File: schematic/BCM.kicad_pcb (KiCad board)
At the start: 2 copper layers, 69 parts, among them P401 POWERCON, P402 KEYSWITCH, P403 CHARGESW, P601 BRUSA_CANCON, P602 A123_CANCON, P603 CON+, P604 CON-, P605 CONPRE, P606 UART, Q1 IRF7101PbF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

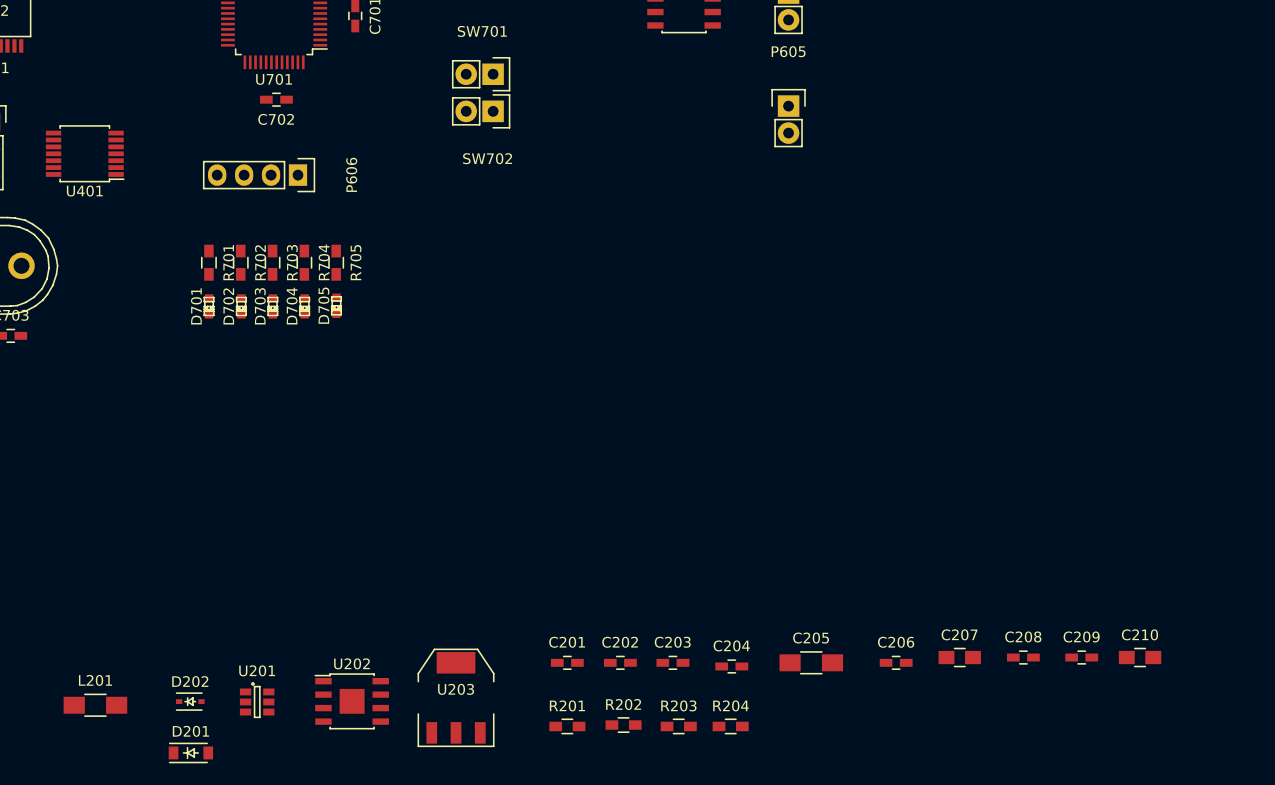
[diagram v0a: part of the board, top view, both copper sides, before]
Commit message: layout: most parts done, fill zones in progress
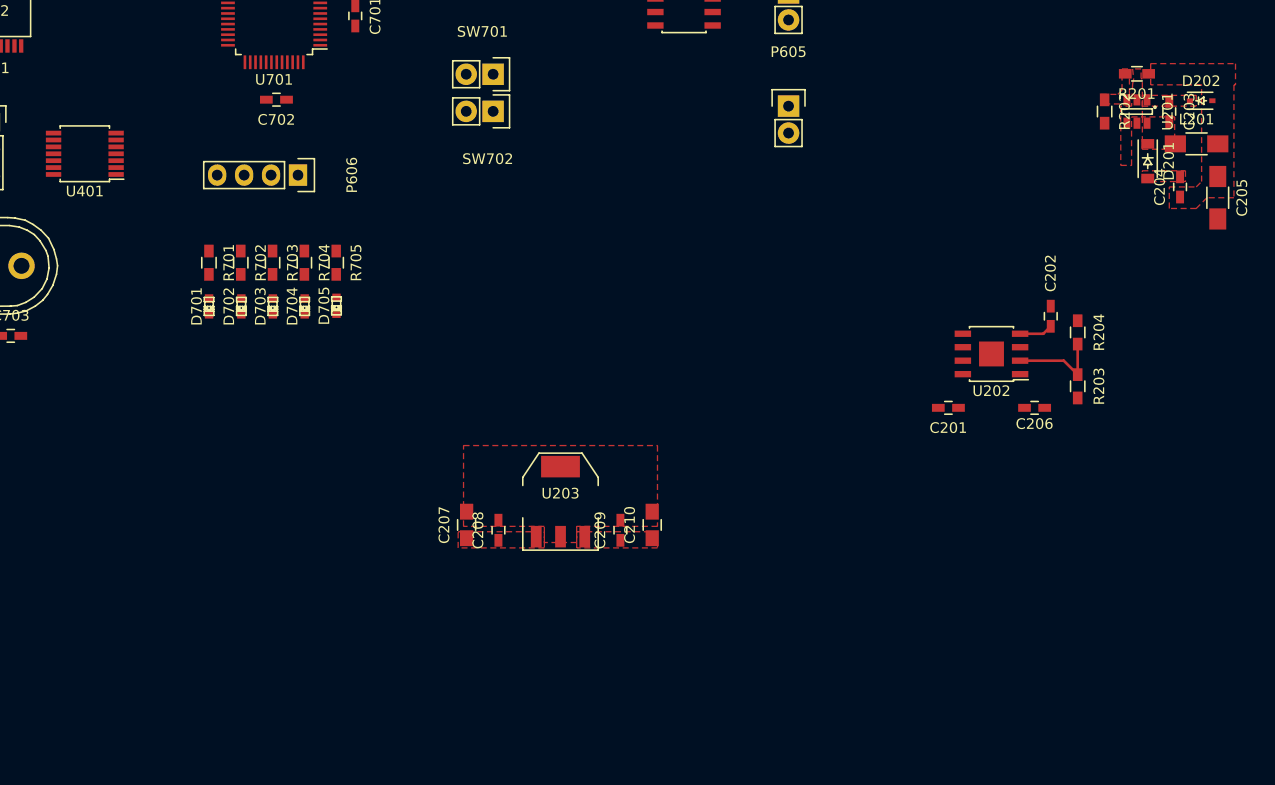
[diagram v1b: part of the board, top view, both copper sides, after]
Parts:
- moved L201 116.5 mm to (209.3, 131.1)
- moved D202 110.9 mm to (209.8, 127.0)
- moved D201 106.1 mm to (204.7, 132.7), turned to 270 degrees
- moved U201 99.9 mm to (203.7, 128.0), turned to 270 degrees
- moved R201 81.7 mm to (203.7, 124.5), turned to 180 degrees
- moved R202 73.5 mm to (200.7, 128.0), turned to 270 degrees
- moved C203 70.0 mm to (206.8, 128.0), turned to 270 degrees
- moved U202 68.6 mm to (190.0, 150.9), turned to 180 degrees
- moved C204 61.9 mm to (207.8, 135.1), turned to 90 degrees
- moved C205 58.2 mm to (211.3, 136.1), turned to 270 degrees
- moved C202 52.1 mm to (195.6, 147.3), turned to 90 degrees
- moved C208 50.9 mm to (143.5, 167.5), turned to 90 degrees
- moved R204 49.5 mm to (198.1, 148.8), turned to 90 degrees
- moved R203 49.4 mm to (198.1, 153.9), turned to 90 degrees
- moved C207 48.2 mm to (140.5, 167.0), turned to 90 degrees
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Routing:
- net /Power/12V0_FB: track 0.00 -> 8.85 mm
- net /Power/12V0_SS: track 0.00 -> 3.18 mm
- added copper zone on F.Cu, net +5V
- added copper zone on F.Cu, net /Power/5V0_BOOST
- added copper zone on F.Cu, net /Power/5V0_FB
- added copper zone on F.Cu, net /Power/5V0_L
- added copper zone on F.Cu, net GND
- added copper zone on F.Cu, net VCC

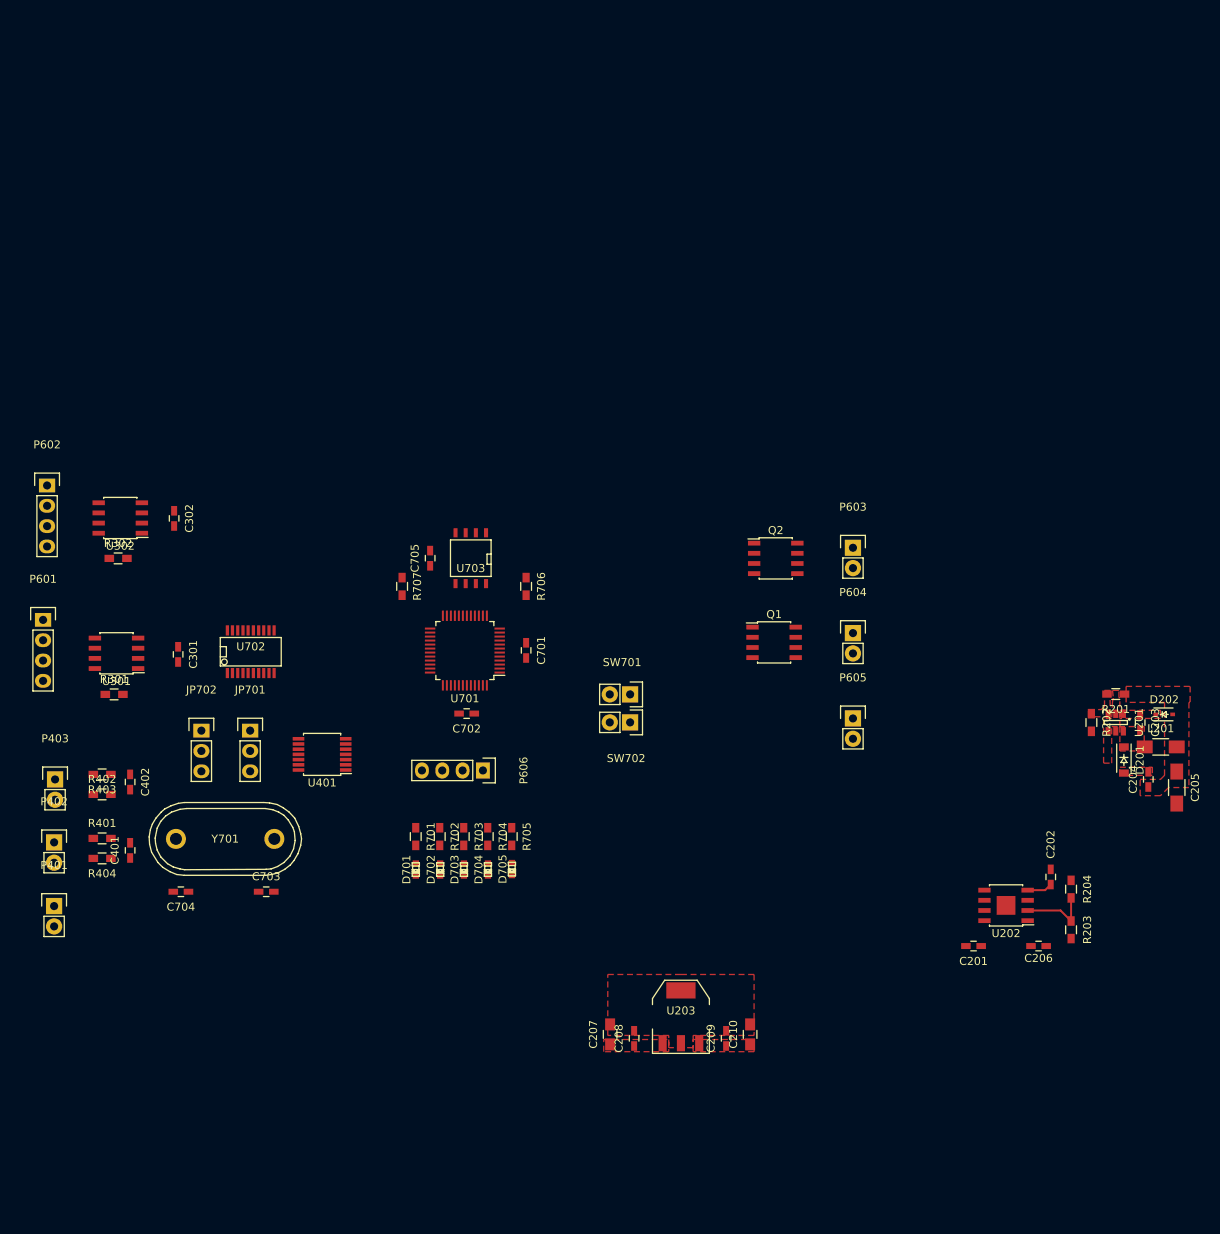
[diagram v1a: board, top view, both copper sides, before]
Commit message: [layout] went to 4 layers nearly done
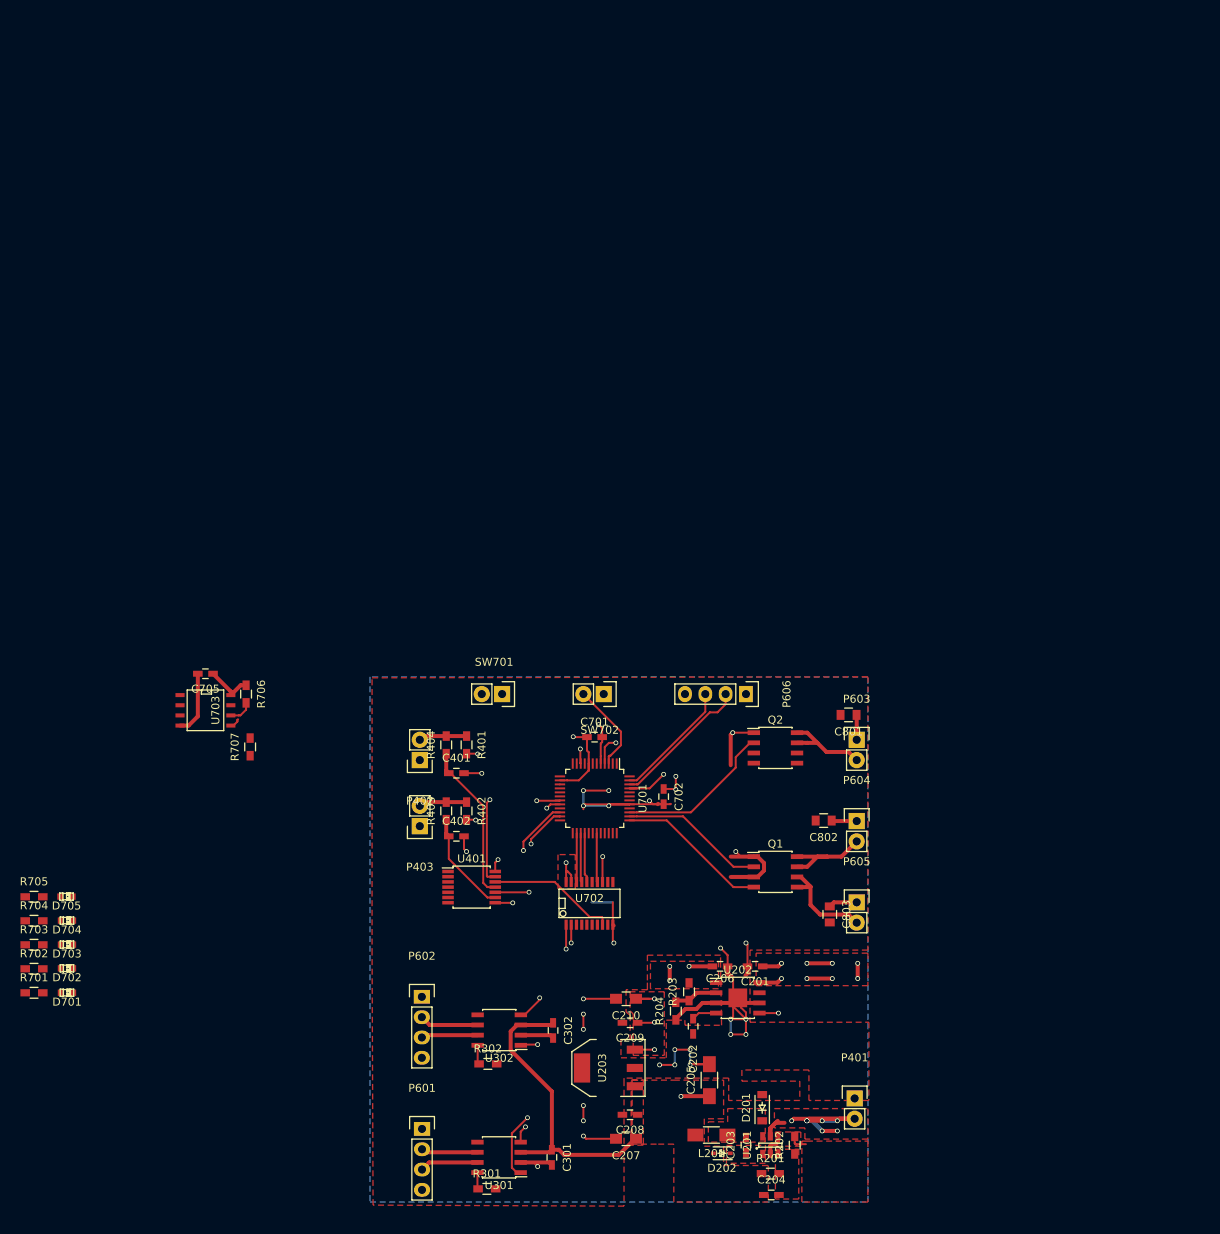
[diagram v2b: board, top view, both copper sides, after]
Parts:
- removed C703, C704: 22p, Capacitors_SMD:C_0603_HandSoldering
- removed JP701, JP702: JUMPER3, Pin_Headers:Pin_Header_Straight_1x03
- removed Y701: 16MHz, Crystals:Crystal_HC48-U_Vertical
- added C801: 10uF, Capacitors_SMD:C_0805, F.Cu at (170.3, 127.1)
- added C802: 10uF, Capacitors_SMD:C_0805, F.Cu at (167.2, 140.3)
- added C803: 10uF, Capacitors_SMD:C_0805, F.Cu at (168.0, 152.0)
- moved P401 102.9 mm to (171.1, 175.0)
- moved C302 79.6 mm to (133.4, 166.5)
- moved U302 79.6 mm to (126.6, 166.5)
- moved P601 79.3 mm to (117.0, 178.8)
- moved P602 79.2 mm to (117.0, 162.3)
- moved U301 79.1 mm to (126.6, 182.4)
- moved C301 78.3 mm to (133.2, 182.4)
- moved R302 78.3 mm to (125.2, 170.7)
- moved D202 77.9 mm to (154.5, 181.9), turned to 180 degrees
- moved R301 77.4 mm to (125.1, 186.3)
- moved L201 74.2 mm to (153.2, 179.6), turned to 180 degrees
- moved R201 73.9 mm to (160.5, 184.4), turned to 0 degrees
- moved C203 72.2 mm to (157.5, 180.8), turned to 90 degrees
- moved C204 70.1 mm to (160.7, 187.1), turned to 0 degrees
- moved C205 68.9 mm to (152.9, 172.7), turned to 90 degrees
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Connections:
- D201 pad 2: /Power/5V0_FB -> GND
- R703 pad 2: /microController/IO_LED01 -> Net-(R703-Pad2)
- U202 pad 9: (no net) -> GND
- U203 pad 4: (no net) -> GND
- U401 pad 1: /Input Connectors/KEYSKWITCH_RC -> (no net)
- U401 pad 10: (no net) -> /microController/KEYSWITCH_IN
- U401 pad 11: (no net) -> /Input Connectors/KEYSKWITCH_RC
- U401 pad 12: (no net) -> /microController/CAN_OSC2
- U401 pad 13: (no net) -> /microController/CLKOUT
- U401 pad 2: /microController/KEYSWITCH_IN -> (no net)
- U401 pad 3: /Input Connectors/CHARGESWITCH_RC -> (no net)
- U401 pad 4: /microController/CHARGESWITCH_IN -> (no net)
- U401 pad 5: /microController/CLKOUT -> (no net)
- U401 pad 6: /microController/CLKOUT_BUFF -> (no net)
- U401 pad 8: (no net) -> /microController/CHARGESWITCH_IN
- U401 pad 9: (no net) -> /Input Connectors/CHARGESWITCH_RC
- U701 pad 11: /Contactor Driver/CON+ -> Net-(U701-Pad11)
- U701 pad 12: /Contactor Driver/CON- -> Net-(U701-Pad12)
- U701 pad 13: /Contactor Driver/CONPRE -> Net-(U701-Pad13)
- U701 pad 22: /microController/KEYSWITCH_IN -> /microController/CHARGESWITCH_IN
- U701 pad 23: /microController/CHARGESWITCH_IN -> /microController/KEYSWITCH_IN
- U701 pad 37: /microController/IO_LED01 -> /Contactor Driver/CONPRE
- U701 pad 38: Net-(U701-Pad38) -> /Contactor Driver/CON-
- U701 pad 39: Net-(U701-Pad39) -> /Contactor Driver/CON+
- U702 pad 9: /microController/CAN_OSC1 -> GND
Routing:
- net GND: track 0.00 -> 148.1 mm, vias 0 -> 29
- net +5V: track 0.00 -> 102.9 mm, vias 0 -> 1
- net +15V: track 0.00 -> 53.5 mm, vias 0 -> 15
- net /Power/EN12V0: track 0.00 -> 44.1 mm, vias 0 -> 2
- net /microController/CLKOUT: track 0.00 -> 43.8 mm, vias 0 -> 2
- net VCC: track 0.00 -> 41.0 mm, vias 0 -> 10
- net /Can transceiver/CAN1_TX: track 0.00 -> 34.5 mm, vias 0 -> 2
- net /Can transceiver/CAN2_TX: track 0.00 -> 34.0 mm, vias 0 -> 2
- net /Can transceiver/CAN2_RX: track 0.00 -> 31.1 mm, vias 0 -> 2
- net /Can transceiver/CAN1_RX: track 0.00 -> 29.8 mm, vias 0 -> 2
- net /Input Connectors/KEYSKWITCH_RC: track 0.00 -> 20.2 mm
- net /microController/CAN1_INT: track 0.00 -> 19.9 mm, vias 0 -> 2
- net /Contactor Driver/CON+: track 0.00 -> 19.9 mm
- net /Contactor Driver/CONPRE: track 0.00 -> 19.5 mm
- net /Contactor Driver/CON-: track 0.00 -> 18.1 mm
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- added copper zone on F.Cu, net +12V
- added copper zone on In1.Cu, net +12V
- added copper zone on F.Cu, net +15V
- added copper zone on In1.Cu, net +15V
- added copper zone on B.Cu, net GND
- added copper zone on In1.Cu, net VCC
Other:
- copper layers 2 -> 4
- net class POWER added: clearance 0.2, trace_width 0.5, via_dia 0.6, via_drill 0.4
